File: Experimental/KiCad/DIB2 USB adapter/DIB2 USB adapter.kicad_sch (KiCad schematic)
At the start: 21 parts, among them X2 10018783-10101TLF, X3 USB1135-15-9-L-B_REVA1

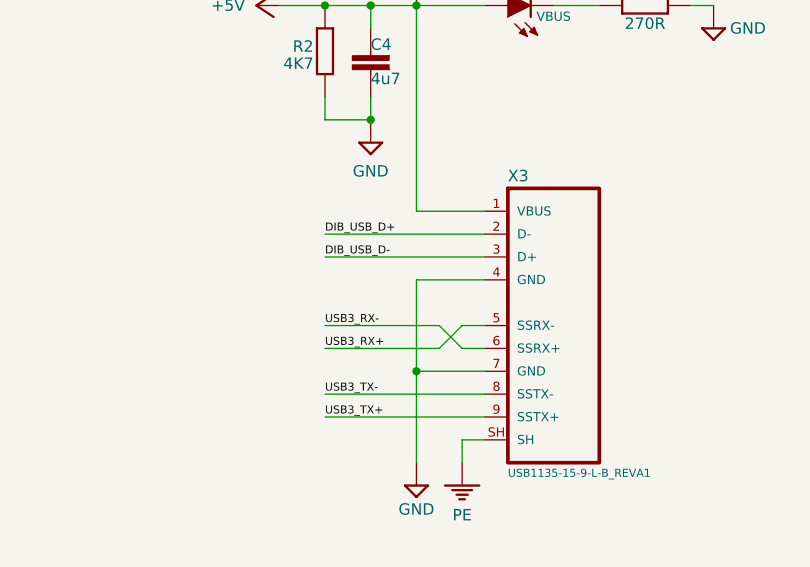
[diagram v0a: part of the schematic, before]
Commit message: USB adapter wiring fixed
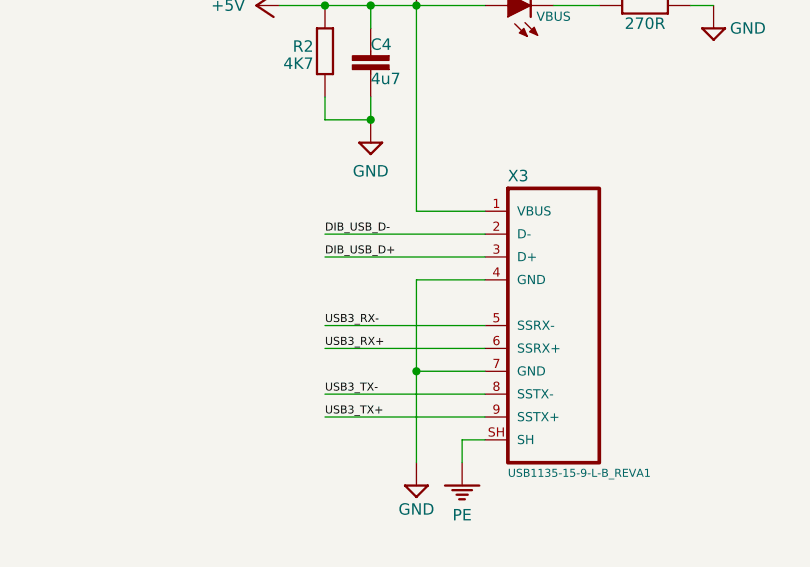
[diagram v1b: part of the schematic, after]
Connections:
- net DIB_USB_D+: now also X3.3 (D+); no longer X3.2 (D-)
- net DIB_USB_D-: now also X3.2 (D-); no longer X3.3 (D+)
- net USB3_RX+: now also X3.6 (SSRX+); no longer X3.5 (SSRX-)
- net USB3_RX-: now also X3.5 (SSRX-); no longer X3.6 (SSRX+)
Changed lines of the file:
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@@
 	(title_block
 		(title "${project_name}")
-		(date "2026-04-04")
+		(date "2026-05-22")
 		(rev "${project_version}")
 		(company "${project_creator}")
@@
 	(wire
 		(pts
+			(xy 160.02 116.84) (xy 177.8 116.84)
+		)
+		(stroke
+			(width 0)
+			(type default)
+		)
+	)
+	(wire
+		(pts
 			(xy 76.2 60.96) (xy 76.2 63.5)
 		)
@@
 	(wire
 		(pts
-			(xy 160.02 116.84) (xy 177.8 116.84)
-		)
-		(stroke
-			(width 0)
-			(type default)
-		)
-	)
-	(wire
-		(pts
 			(xy 175.26 48.26) (xy 177.8 48.26)
 		)
@@
 	(wire
 		(pts
-			(xy 172.72 127) (xy 175.26 124.46)
-		)
-		(stroke
-			(width 0)
-			(type default)
-		)
-	)
-	(wire
-		(pts
 			(xy 190.5 68.58) (xy 198.12 68.58)
 		)
@@
 	(wire
 		(pts
-			(xy 175.26 124.46) (xy 177.8 124.46)
-		)
-		(stroke
-			(width 0)
-			(type default)
-		)
-	)
-	(wire
-		(pts
 			(xy 78.74 60.96) (xy 76.2 60.96)
 		)
@@
 	(wire
 		(pts
+			(xy 160.02 114.3) (xy 177.8 114.3)
+		)
+		(stroke
+			(width 0)
+			(type default)
+		)
+	)
+	(wire
+		(pts
 			(xy 30.48 109.22) (xy 43.18 109.22)
 		)
@@
 	(wire
 		(pts
-			(xy 172.72 124.46) (xy 175.26 127)
-		)
-		(stroke
-			(width 0)
-			(type default)
-		)
-	)
-	(wire
-		(pts
 			(xy 73.66 68.58) (xy 73.66 78.74)
 		)
@@
 	(wire
 		(pts
-			(xy 175.26 127) (xy 177.8 127)
-		)
-		(stroke
-			(width 0)
-			(type default)
-		)
-	)
-	(wire
-		(pts
 			(xy 205.74 43.18) (xy 205.74 50.8)
 		)
@@
 	(wire
 		(pts
-			(xy 160.02 127) (xy 172.72 127)
+			(xy 160.02 127) (xy 177.8 127)
 		)
 		(stroke
@@
 	(wire
 		(pts
-			(xy 160.02 124.46) (xy 172.72 124.46)
+			(xy 160.02 124.46) (xy 177.8 124.46)
 		)
 		(stroke
@@
 		(pts
 			(xy 165.1 53.34) (xy 177.8 53.34)
-		)
-		(stroke
-			(width 0)
-			(type default)
-		)
-	)
-	(wire
-		(pts
-			(xy 160.02 114.3) (xy 177.8 114.3)
 		)
 		(stroke
@@
 	)
 	(label "DIB_USB_D+"
-		(at 160.02 114.3 0)
+		(at 160.02 116.84 0)
 		(effects
 			(font
@@
 	)
 	(label "DIB_USB_D-"
-		(at 160.02 116.84 0)
-		(effects
-			(font
+		(at 160.02 114.3 0)
+		(effects
+			(font
